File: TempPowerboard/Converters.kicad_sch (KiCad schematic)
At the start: 47 parts, among them IC2 LMR23630ADDA, IC3 TPS25810RVCT, IC4 LMR23630ADDA, IC5 LT3080IST#WPBF, J3 USB_C_Receptacle_USB2.0, SW1 SW_DIP_x01

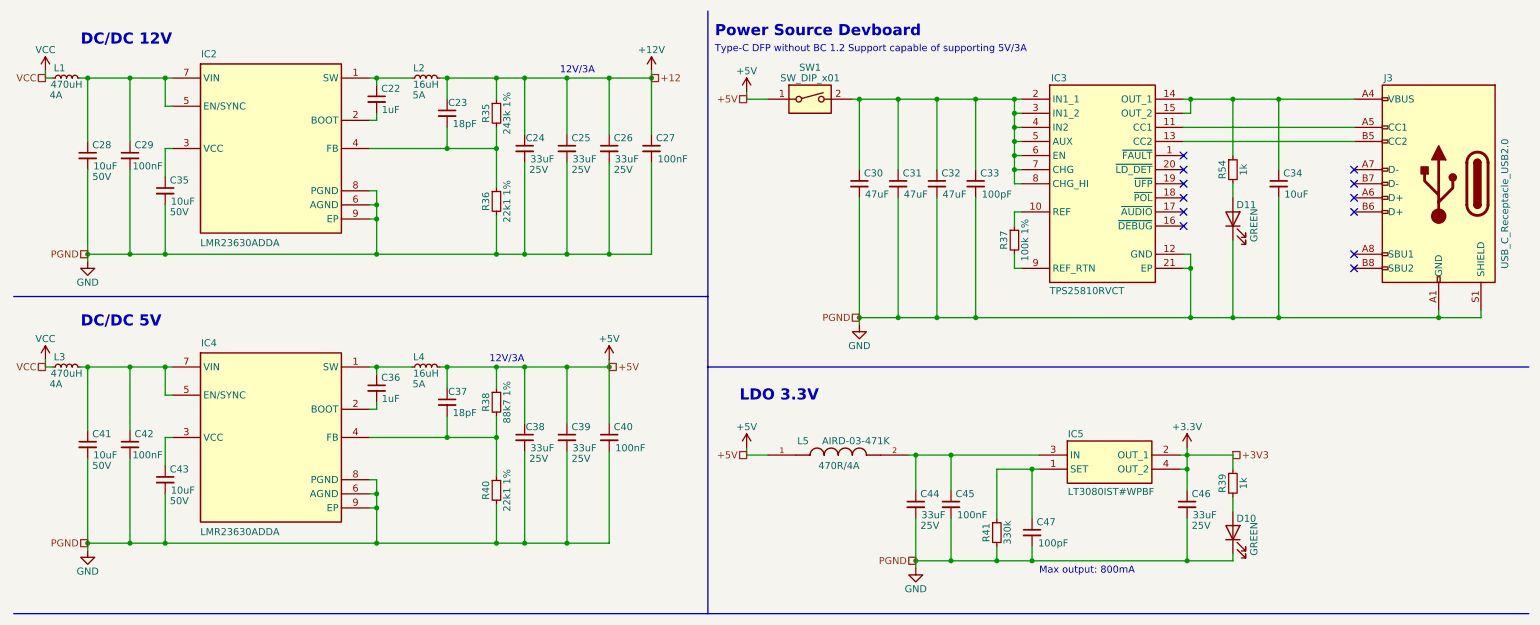
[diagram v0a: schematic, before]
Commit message: Devboard ports defined
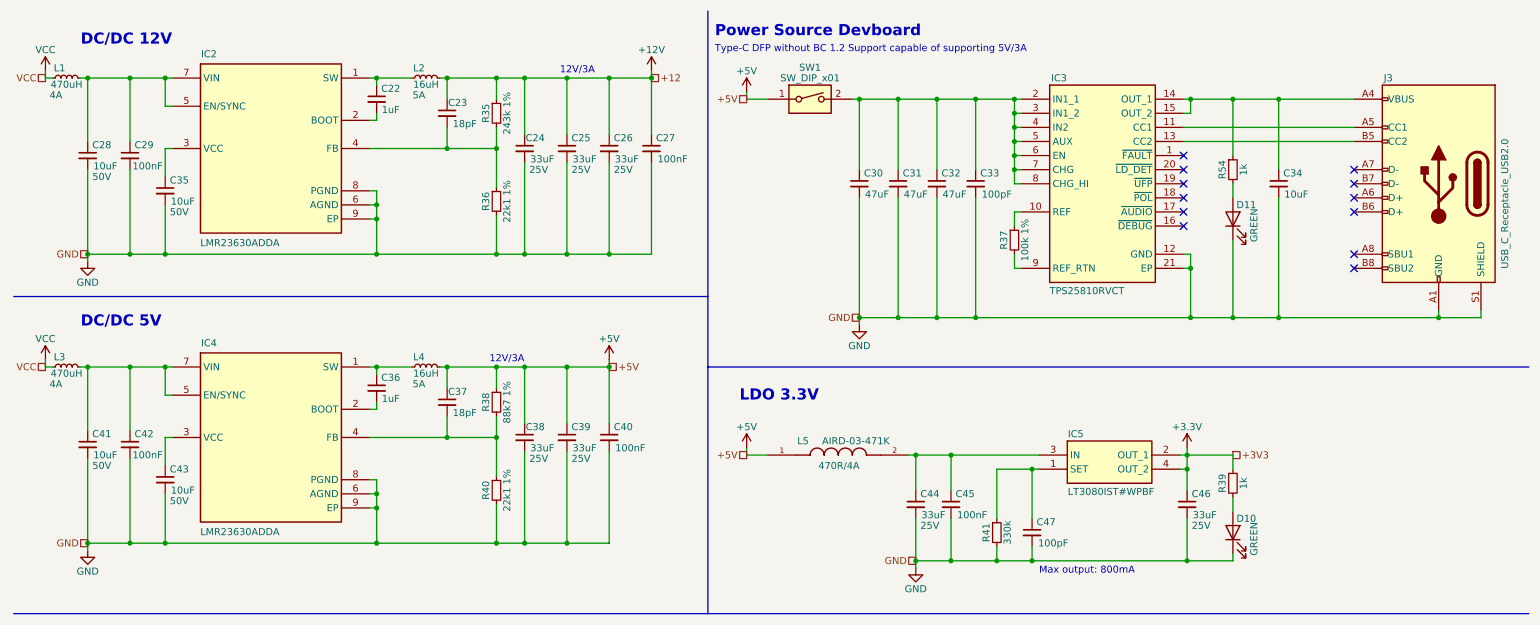
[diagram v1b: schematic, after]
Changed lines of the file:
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@@
     (effects (font (size 1.27 1.27)) (justify left))
   )
-  (hierarchical_label "PGND" (shape passive) (at 174.625 111.125 180) (fields_autoplaced)
+  (hierarchical_label "GND" (shape passive) (at 174.625 111.125 180) (fields_autoplaced)
     (effects (font (size 1.27 1.27)) (justify right))
   )
-  (hierarchical_label "PGND" (shape passive) (at 164.465 67.31 180) (fields_autoplaced)
+  (hierarchical_label "GND" (shape passive) (at 164.465 67.31 180) (fields_autoplaced)
     (effects (font (size 1.27 1.27)) (justify right))
   )
@@
     (effects (font (size 1.27 1.27)) (justify right))
   )
-  (hierarchical_label "PGND" (shape passive) (at 25.4 55.88 180) (fields_autoplaced)
+  (hierarchical_label "GND" (shape passive) (at 25.4 55.88 180) (fields_autoplaced)
     (effects (font (size 1.27 1.27)) (justify right))
   )
@@
     (effects (font (size 1.27 1.27)) (justify left))
   )
-  (hierarchical_label "PGND" (shape passive) (at 25.4 107.95 180) (fields_autoplaced)
+  (hierarchical_label "GND" (shape passive) (at 25.4 107.95 180) (fields_autoplaced)
     (effects (font (size 1.27 1.27)) (justify right))
   )
